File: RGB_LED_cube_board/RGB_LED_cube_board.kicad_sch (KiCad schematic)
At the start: 32 parts

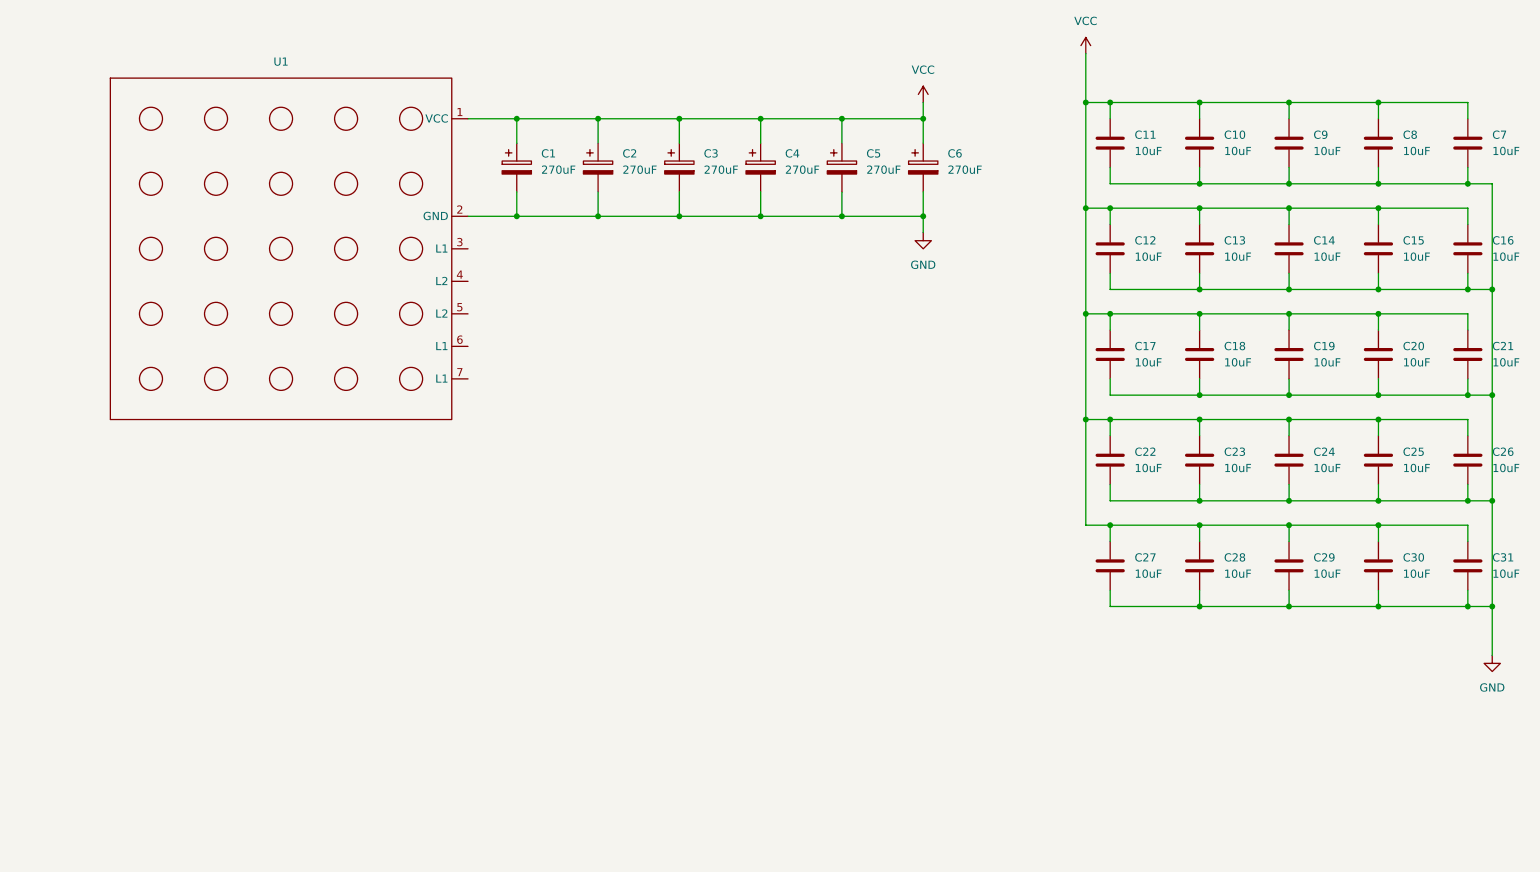
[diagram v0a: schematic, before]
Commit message: Finished layout, created the footprint for the led cube. The xt30 connector needs some attention to its location and the vias aroud it.
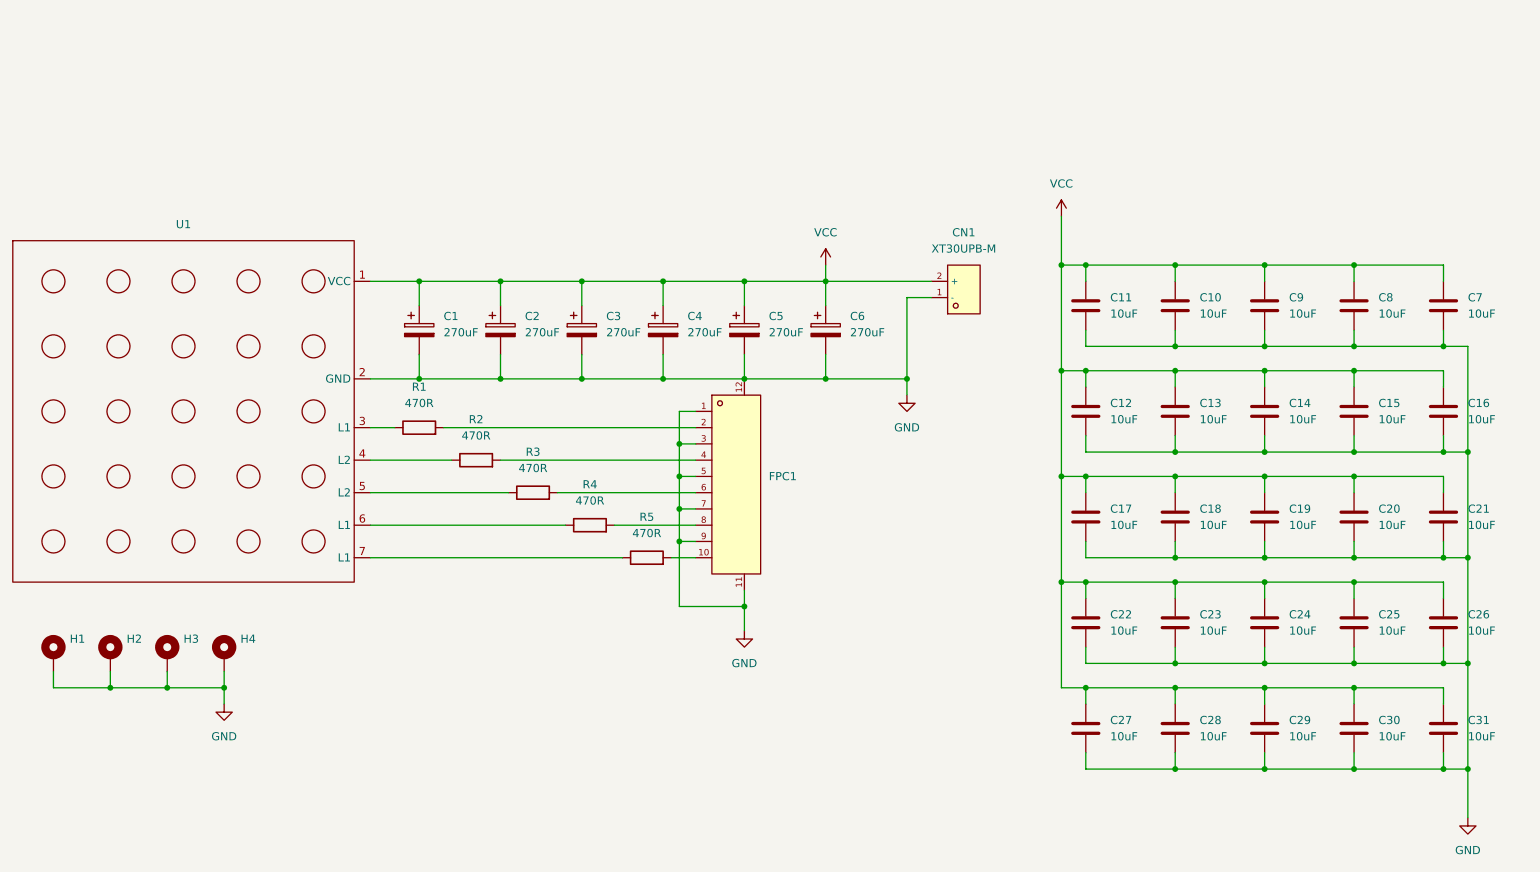
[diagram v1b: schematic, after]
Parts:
- added CN1: XT30UPB-M, lcsc_footprints:C428721_CONN-TH_XT30UPB-M, symbol lcsc_imported:XT30UPB-M
- added FPC1: XW05202-100R-00, lcsc_footprints:C2906114_FPC-SMD_10P-P0_50_HCTL_XW05202-100R-00, symbol lcsc_imported:XW05202-100R-00
- added H1, H2, H3, H4: MountingHole_Pad, MountingHole:MountingHole_3.2mm_M3_Pad_Via, symbol Mechanical:MountingHole_Pad
- added R1, R2, R3, R4, R5: 470R, Resistor_SMD:R_0402_1005Metric_Pad0.72x0.64mm_HandSolder, symbol Device:R
- U1: footprint (none) -> custom:LED_CUBE_RGB_5x5x5
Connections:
- net GND: now also CN1.1 (-), FPC1.1, FPC1.11, FPC1.12, FPC1.3, FPC1.5, FPC1.7, FPC1.9, H1.1, H2.1, H3.1, H4.1
- net VCC: now also CN1.2 (+)
- net at U1.3 (L1): now also R1.1
- net at U1.4 (L2): now also R2.1
- net at U1.5 (L2): now also R3.1
- net at U1.6 (L1): now also R4.1
- net at U1.7 (L1): now also R5.1
- new net: FPC1.10, R5.2
- new net: FPC1.2, R1.2
- new net: FPC1.8, R4.2
- new net: FPC1.6, R3.2
- new net: FPC1.4, R2.2
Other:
- moved on the sheet: C1, C10, C11, C12, C13, C14, C15, C16, C17, C18, C19, C2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
